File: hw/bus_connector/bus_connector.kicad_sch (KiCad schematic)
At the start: 11 parts, among them J1 DB9_Top, J2 DB9_Right, J3 DB9_Left

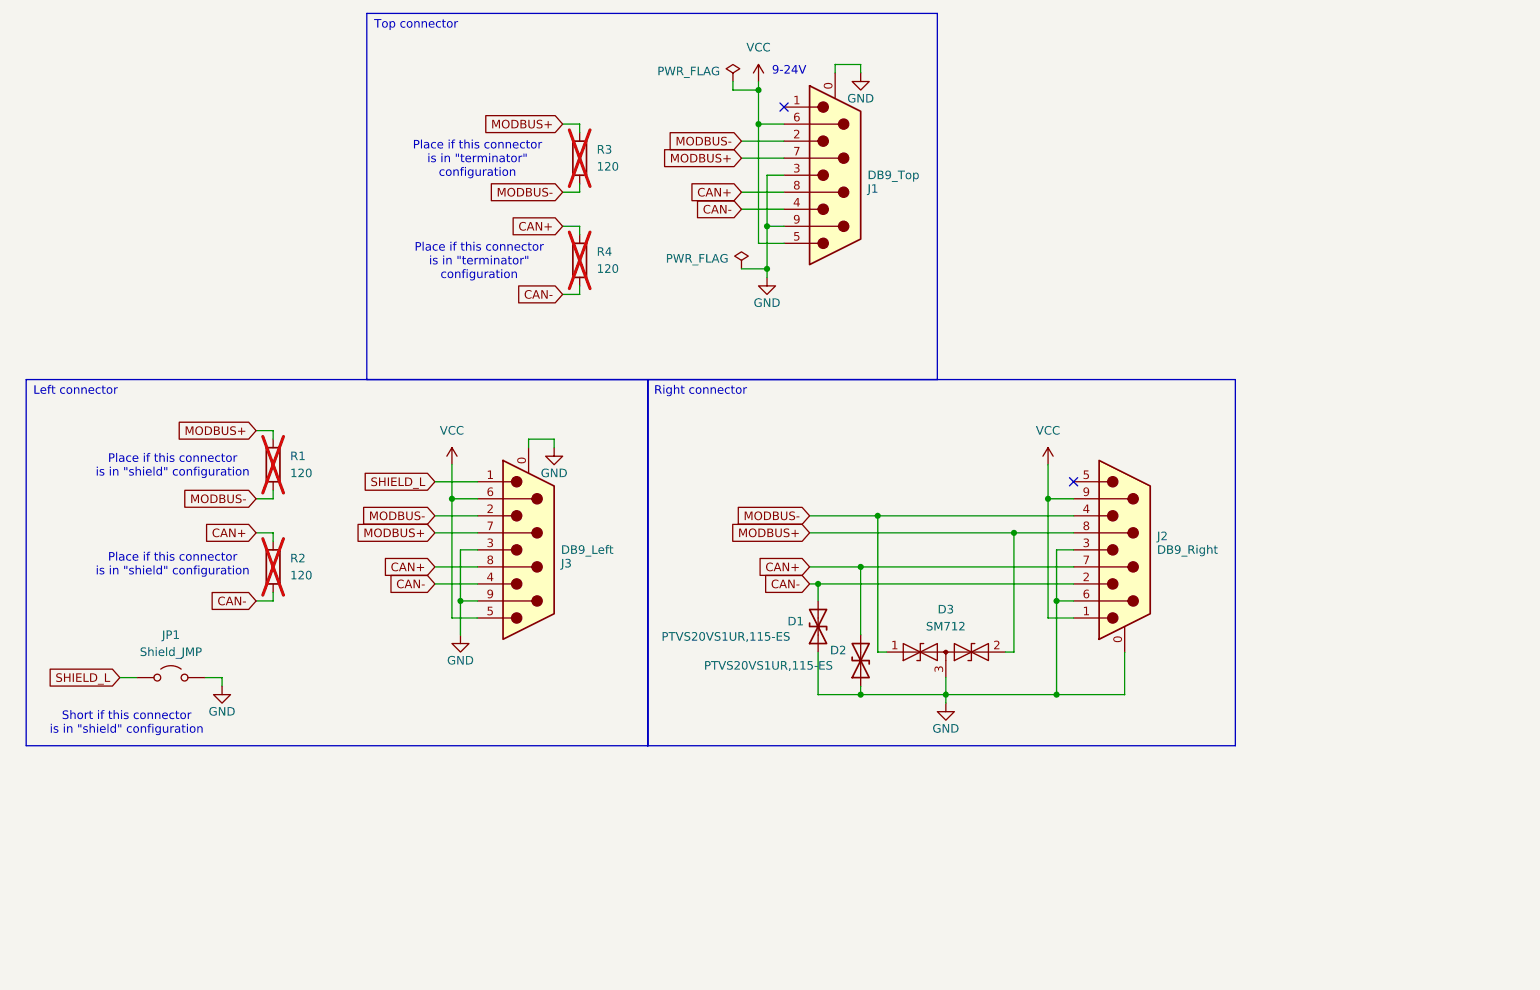
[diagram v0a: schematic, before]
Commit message: Fix schematic labels
Signed-off-by: Mateusz Pająk <22417805+Tai-Min@users.noreply.github.com>
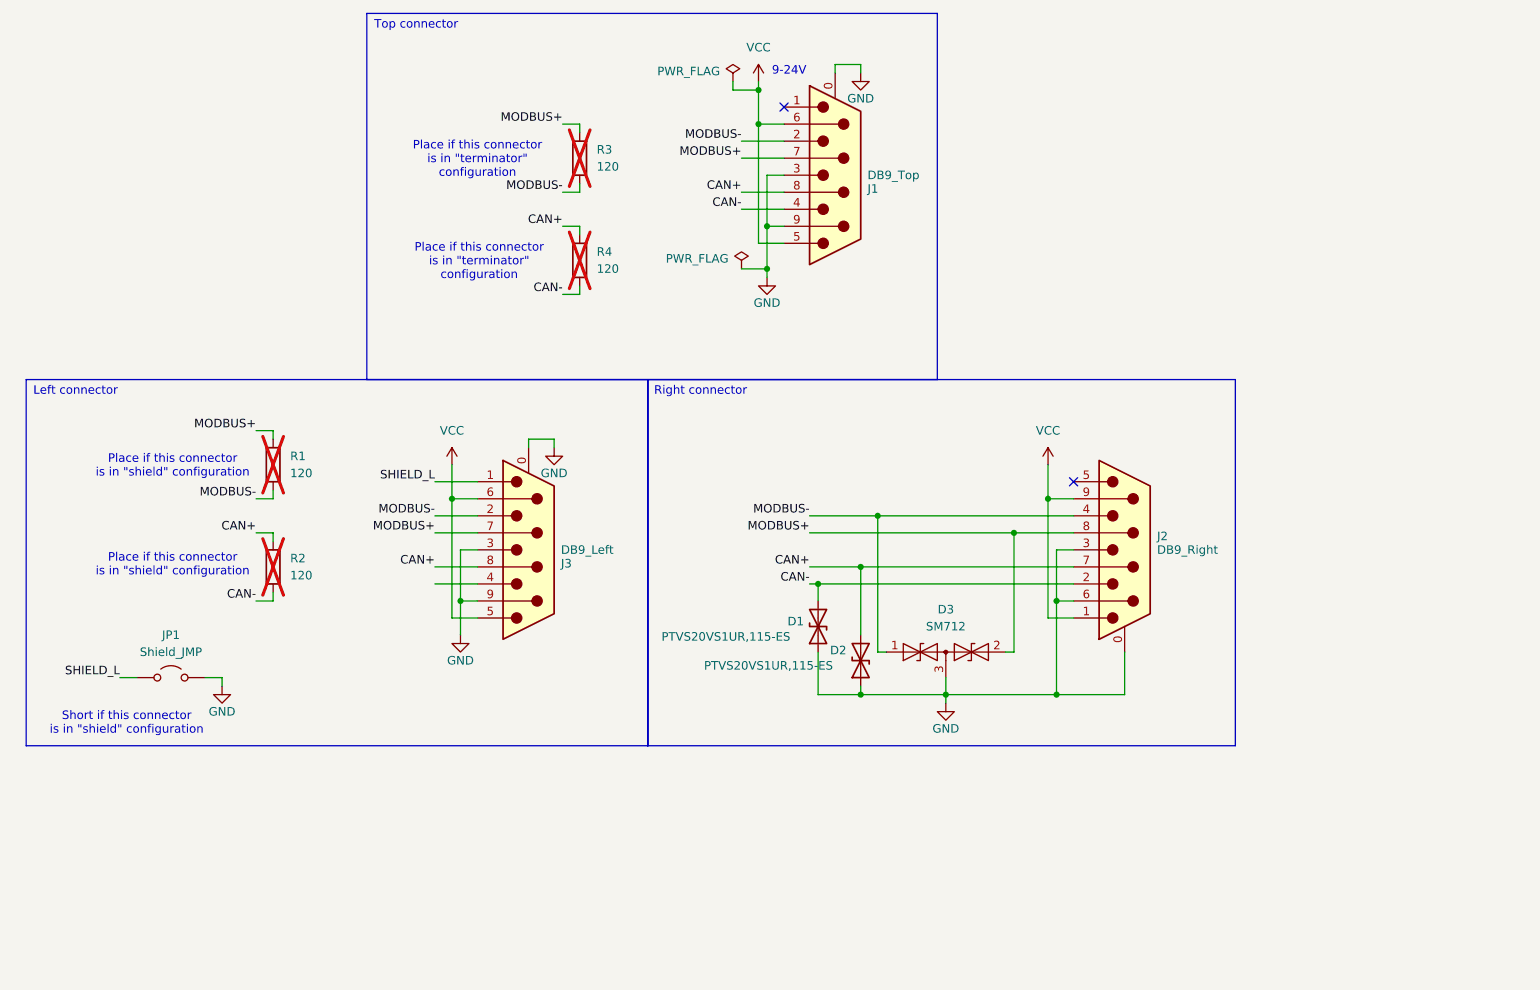
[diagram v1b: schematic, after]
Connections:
- net CAN-: no longer J3.4

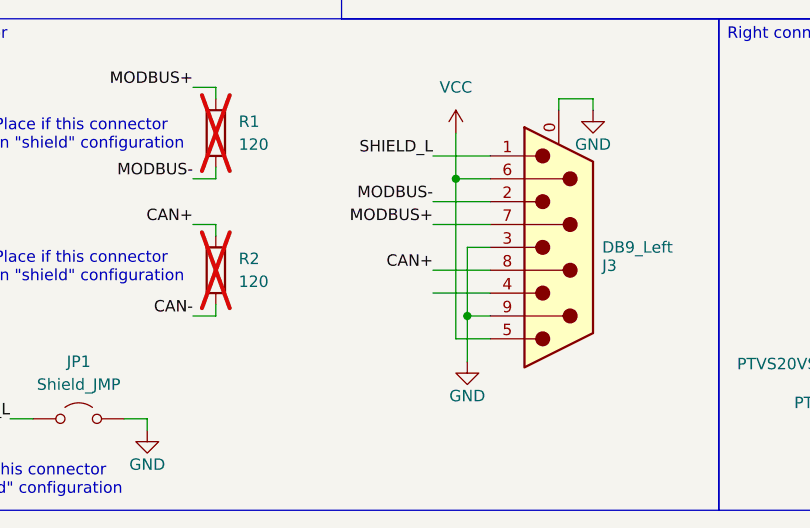
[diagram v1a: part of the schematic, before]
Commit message: Fix parity issues
Signed-off-by: Mateusz Pająk <22417805+Tai-Min@users.noreply.github.com>
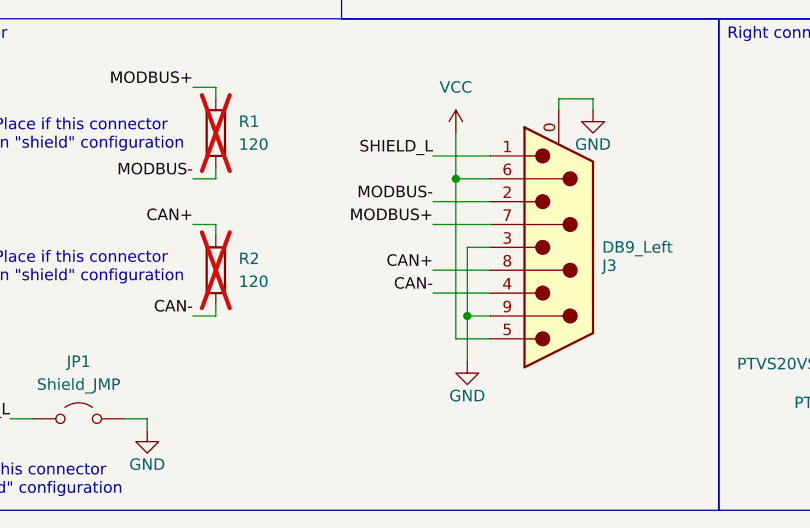
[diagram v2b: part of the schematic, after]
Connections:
- net CAN-: now also J3.4
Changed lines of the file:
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@@
+	)
+	(label "CAN-"
+		(at 120.65 121.92 180)
+		(effects
+			(font
+				(size 1.27 1.27)
+			)
+			(justify right bottom)
+		)
 	)
 	(label "CAN-"

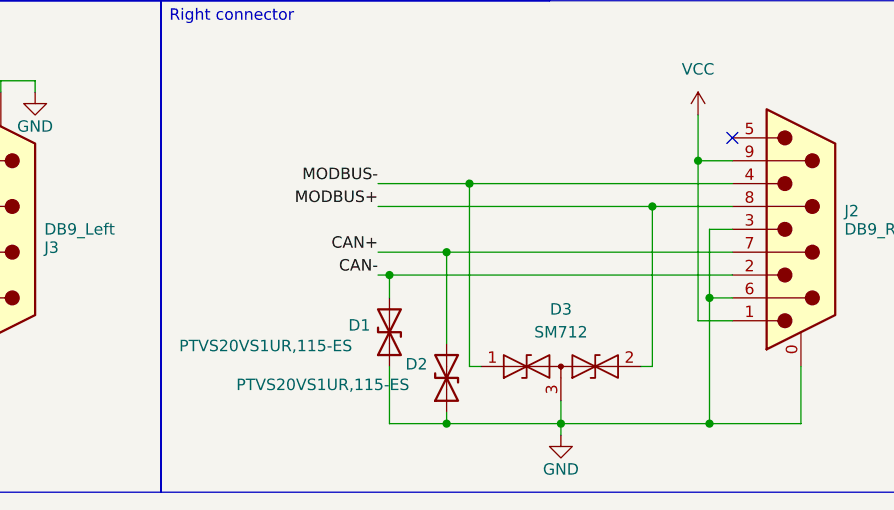
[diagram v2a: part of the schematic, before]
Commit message: Tracks for left panel rerouted, tvs diode replaced, more vias added
Signed-off-by: Mateusz Pająk <22417805+Tai-Min@users.noreply.github.com>
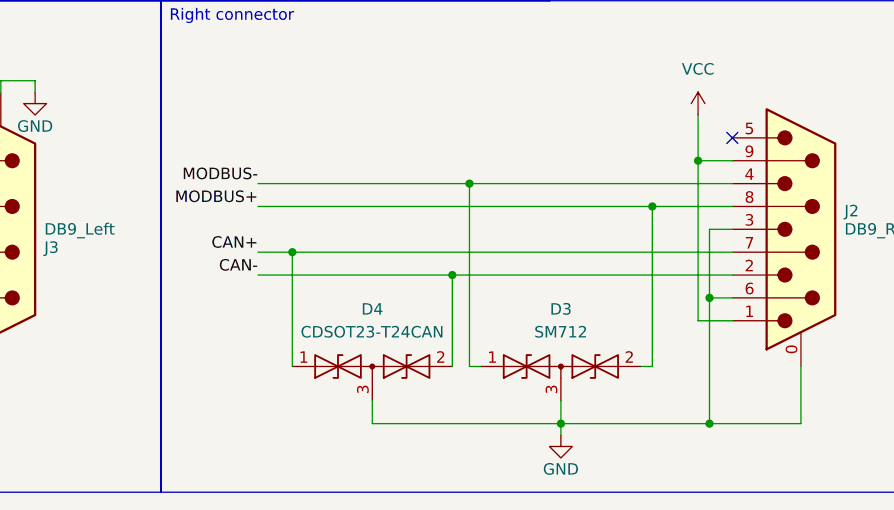
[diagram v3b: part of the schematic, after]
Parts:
- removed D1, D2: PTVS20VS1UR,115-ES, Diode_SMD:D_SOD-123F, symbol Device:D_TVS
- added D4: CDSOT23-T24CAN, Package_TO_SOT_SMD:SOT-23, symbol Diode:SM712_SOT23
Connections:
- net CAN+: now also D4.1 (A1)
- net CAN-: now also D4.2 (A2)
- net GND: now also D4.3 (common)

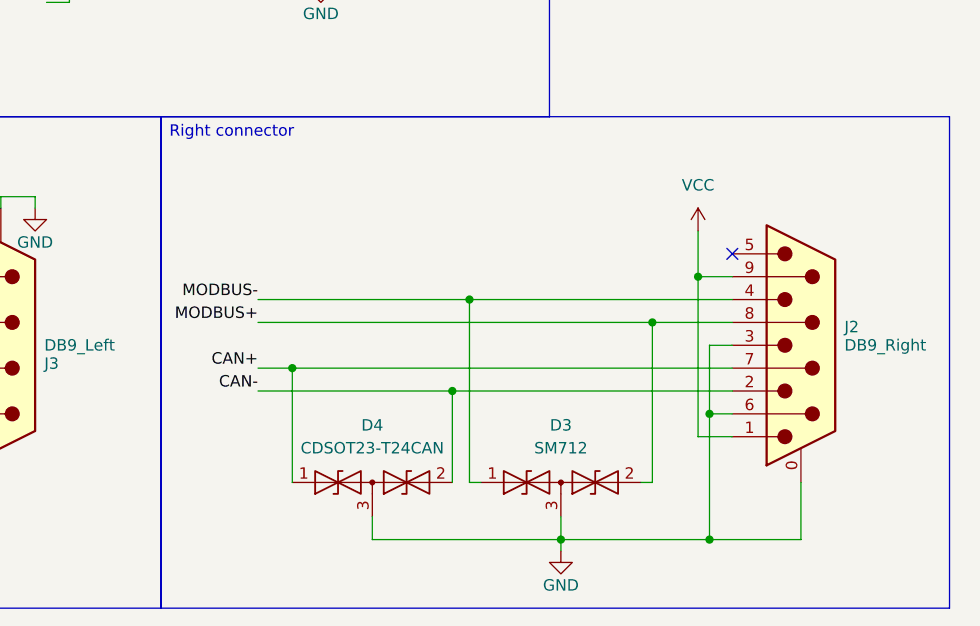
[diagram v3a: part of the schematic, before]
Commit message: Fix silkscreen, fix thermal error, add via array
Signed-off-by: Mateusz Pająk <22417805+Tai-Min@users.noreply.github.com>
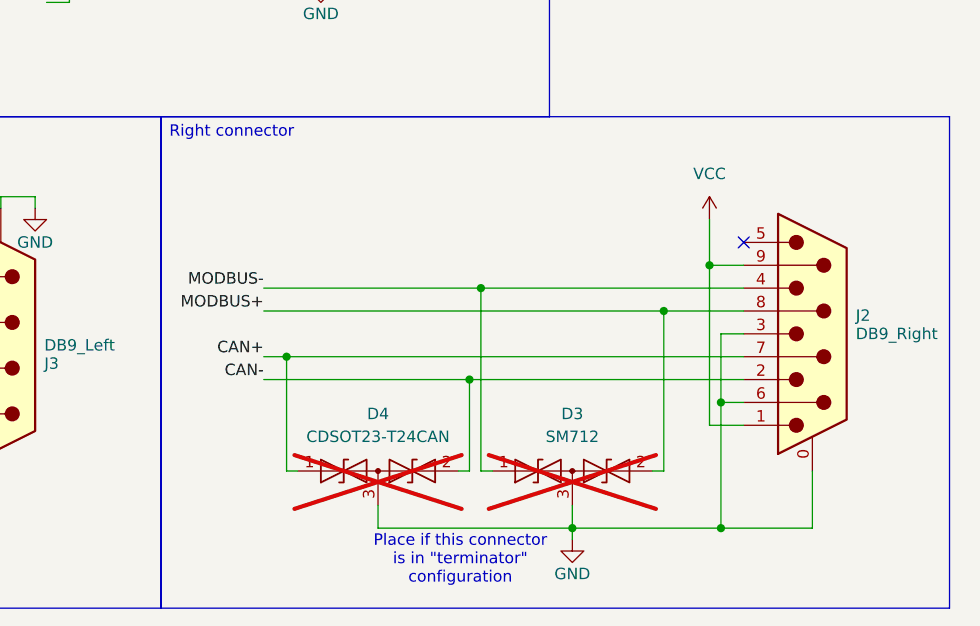
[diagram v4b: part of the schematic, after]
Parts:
- D3, D4: now not fitted
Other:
- moved on the sheet: J2
